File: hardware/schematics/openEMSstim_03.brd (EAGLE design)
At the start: 38 x 59 mm, 37 parts

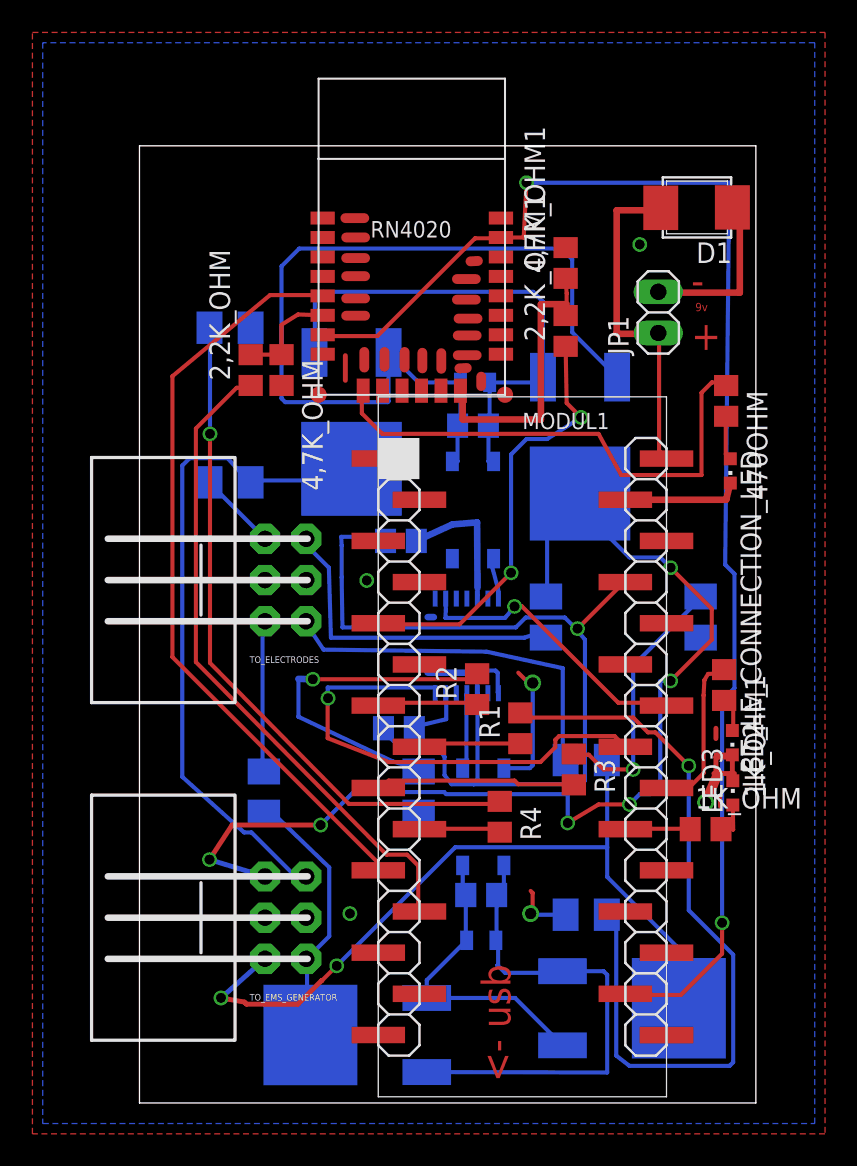
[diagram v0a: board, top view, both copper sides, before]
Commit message: new board design V3: not tested yet
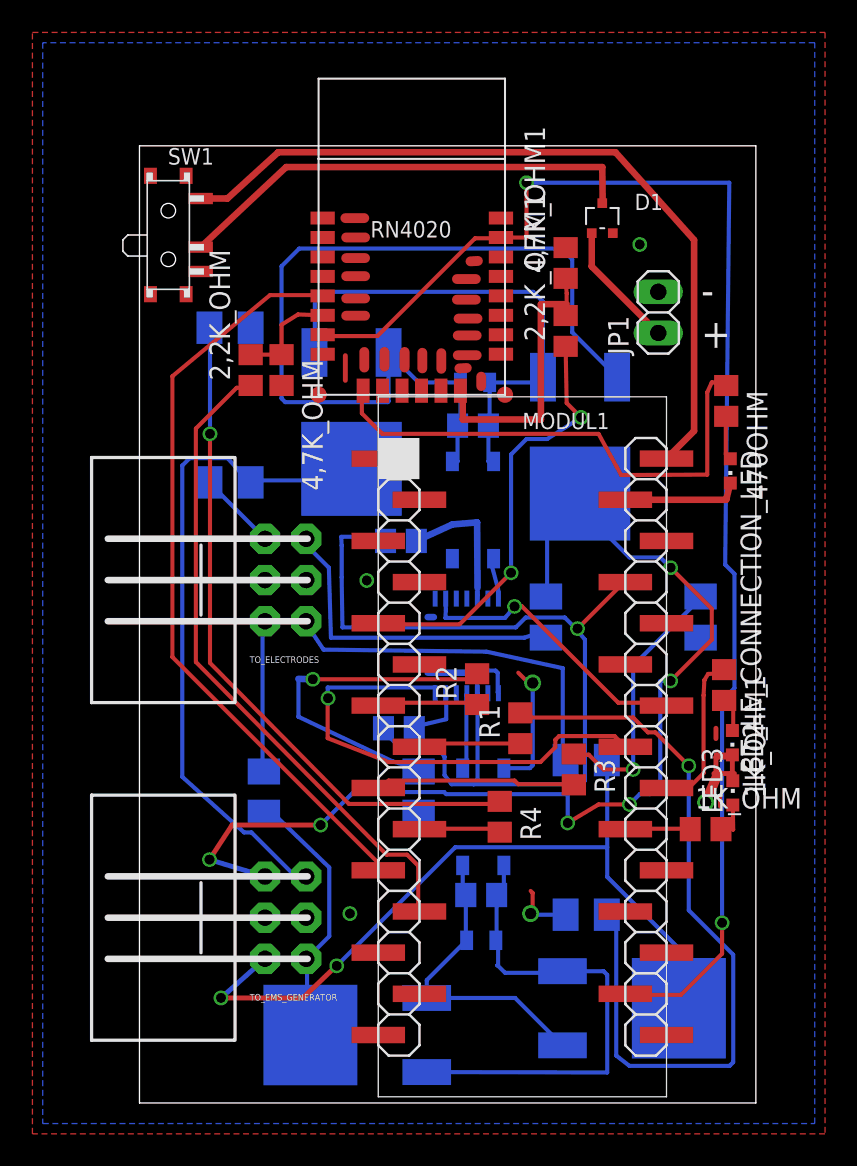
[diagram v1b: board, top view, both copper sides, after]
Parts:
- added SW1: SW1, alps:SSSS810701
- D1: value 1N4001 -> 1PS70SB10; device semicon-smd-ipc:SMB -> nxp_60:SOT323
- moved D1 5.74 mm to (32.6, 54.6), turned to 0 degrees
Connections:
- new net N$64: D1.3, SW1.2
- net N$11: now also SW1.1; no longer D1.1
- net N$63: now also D1.1; no longer D1.2
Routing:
- net N$11: track 7.76 -> 48.1 mm
- net N$64: track 12.5 -> 29.0 mm
- net N$65: track 10.8 -> 0.00 mm
- net N$63: track 0.00 -> 7.86 mm
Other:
- board text added: "- +"
- board text added: "open EMS stim"
- board text added: "openEMSstim v2 plopes.org/ems"
- board text removed: "+"
- board text removed: "-"
- board text removed: "9v"
- board text removed: "<- usb"
- board text removed: "openEMSstim 0.2 by Pedro Lopes plopes.org/ems open source control board for EMS units based on toolkit by Pfeiffer & Duente v0.1"
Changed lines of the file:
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@@
 <layer number="112" name="tSilk" color="7" fill="1" visible="no" active="yes"/>
 <layer number="113" name="IDFDebug" color="7" fill="1" visible="no" active="yes"/>
+<layer number="114" name="FRNTMAAT1" color="7" fill="1" visible="yes" active="yes"/>
+<layer number="115" name="FRNTMAAT2" color="7" fill="1" visible="yes" active="yes"/>
 <layer number="116" name="Patch_BOT" color="9" fill="4" visible="no" active="yes"/>
+<layer number="117" name="BACKMAAT1" color="7" fill="1" visible="yes" active="yes"/>
 <layer number="118" name="Rect_Pads" color="7" fill="1" visible="no" active="no"/>
+<layer number="119" name="KAP_TEKEN" color="7" fill="1" visible="yes" active="yes"/>
+<layer number="120" name="KAP_MAAT1" color="7" fill="1" visible="yes" active="yes"/>
 <layer number="121" name="_tsilk" color="7" fill="1" visible="no" active="yes"/>
 <layer number="122" name="_bsilk" color="7" fill="1" visible="no" active="yes"/>
@@
 <layer number="128" name="_bValues" color="7" fill="1" visible="no" active="yes"/>
 <layer number="129" name="Mask" color="7" fill="1" visible="no" active="yes"/>
+<layer number="130" name="SMDSTROOK" color="7" fill="1" visible="yes" active="yes"/>
 <layer number="131" name="tAdjust" color="7" fill="1" visible="no" active="yes"/>
 <layer number="132" name="bAdjust" color="7" fill="1" visible="no" active="yes"/>
@@
 <text x="5.461" y="0.889" size="1.778" layer="126" rot="MR90">HCI - Hannover</text>
 <text x="40.64" y="58.039" size="1.778" layer="126" rot="MR270">V002 EMS WS Module</text>
-<text x="4.8514" y="52.6288" size="0.508" layer="104" font="vector" ratio="9">openEMSstim 0.2
-by Pedro Lopes
-plopes.org/ems
-open source control
-board for EMS units
-based on toolkit by
-Pfeiffer &amp; Duente v0.1</text>
-<text x="38.1" y="46.4566" size="1.778" layer="1">+</text>
-<text x="38.1" y="49.8602" size="1.778" layer="1">-</text>
-<text x="38.354" y="48.8442" size="0.508" layer="1">9v</text>
-<text x="26.9494" y="1.2954" size="1.778" layer="1" rot="R90">&lt;- usb </text>
+<text x="35.5854" y="57.2516" size="0.508" layer="104" font="vector" ratio="9">openEMSstim v2
+plopes.org/ems</text>
+<text x="4.4704" y="19.5326" size="1.27" layer="104">open
+EMS
+stim</text>
+<text x="38.7096" y="46.5836" size="1.778" layer="21">-
++</text>
 </plain>
 <attributes>
@@
 <element name="C1" library="SparkFun-Passives" package="0805" value="100nf" x="25.146" y="10.033" rot="MR0"/>
 <element name="C3" library="SparkFun-Passives" package="0805" value="100nf" x="24.765" y="44.45" rot="MR0"/>
-<element name="D1" library="semicon-smd-ipc" package="SMB" value="1N4001" x="38.3286" y="55.118" rot="R180"/>
+<element name="D1" library="nxp_60" package="SOT323" value="1PS70SB10" x="32.6136" y="54.5846"/>
+<element name="SW1" library="alps" package="SSSS810701" value="SW1" x="5.842" y="53.5432" smashed="yes" rot="R270">
+<attribute name="NAME" x="5.8166" y="57.8866" size="1.016" layer="25"/>
+</element>
 </elements>
 <signals>
@@
 <via x="27.94" y="56.769" extent="1-16" drill="0.6096"/>
 <wire x1="18.7325" y1="47.3075" x2="24.765" y2="53.34" width="0.254" layer="1"/>
-<wire x1="26.363" y1="53.388" x2="27.765" y2="53.388" width="0.254" layer="1"/>
-<wire x1="27.765" y1="53.388" x2="27.94" y2="56.769" width="0.254" layer="1"/>
+<wire x1="26.363" y1="53.388" x2="27.9428" y2="53.388" width="0.254" layer="1"/>
+<wire x1="27.9428" y1="53.388" x2="27.94" y2="56.769" width="0.254" layer="1"/>
 <wire x1="40.4495" y1="56.769" x2="40.1955" y2="33.2105" width="0.254" layer="16"/>
 <wire x1="40.1955" y1="33.2105" x2="40.767" y2="32.639" width="0.254" layer="16"/>
@@
 <signal name="N$11">
 <contactref element="MODUL1" pad="30"/>
-<wire x1="36.1188" y1="40.2336" x2="36.1188" y2="47.3202" width="0.254" layer="1"/>
-<wire x1="36.576" y1="39.7764" x2="36.1188" y2="40.2336" width="0.254" layer="1"/>
-<wire x1="36.576" y1="39.7764" x2="36.576" y2="39.751" width="0.254" layer="1"/>
-<contactref element="D1" pad="1"/>
-<wire x1="40.64" y1="55.245" x2="36.576" y2="39.751" width="0" layer="19" extent="1-1"/>
+<contactref element="SW1" pad="1"/>
+<wire x1="7.842" y1="55.7932" x2="9.489" y2="55.7932" width="0.4064" layer="1"/>
+<wire x1="9.489" y1="55.7932" x2="12.6238" y2="58.6486" width="0.4064" layer="1"/>
+<wire x1="12.6238" y1="58.6486" x2="33.4264" y2="58.6486" width="0.4064" layer="1"/>
+<wire x1="33.4264" y1="58.6486" x2="38.2778" y2="53.2384" width="0.4064" layer="1"/>
+<wire x1="38.2778" y1="53.2384" x2="38.2778" y2="41.4528" width="0.4064" layer="1"/>
+<wire x1="38.2778" y1="41.4528" x2="36.576" y2="39.751" width="0.4064" layer="1"/>
 </signal>
 <signal name="N$17">
@@
 <wire x1="32.385" y1="41.275" x2="19.05" y2="41.275" width="0.254" layer="1"/>
 <wire x1="33.782" y1="38.735" x2="32.385" y2="41.275" width="0.254" layer="1"/>
-<wire x1="38.735" y1="38.735" x2="33.782" y2="38.735" width="0.254" layer="1"/>
-<wire x1="38.735" y1="43.815" x2="38.735" y2="38.735" width="0.254" layer="1"/>
-<wire x1="39.37" y1="44.45" x2="38.735" y2="43.815" width="0.254" layer="1"/>
+<wire x1="39.0906" y1="38.7604" x2="33.782" y2="38.735" width="0.254" layer="1"/>
+<wire x1="39.0906" y1="43.8404" x2="39.0906" y2="38.7604" width="0.254" layer="1"/>
+<wire x1="39.37" y1="44.45" x2="39.0906" y2="43.8404" width="0.254" layer="1"/>
 <wire x1="40.005" y1="44.45" x2="39.37" y2="44.45" width="0.254" layer="1"/>
 <wire x1="17.78" y1="43.815" x2="17.863" y2="43.938" width="0.254" layer="1"/>
@@
 <wire x1="18.0848" y1="32.1818" x2="18.0848" y2="32.2326" width="0.4064" layer="1"/>
 <wire x1="12.827" y1="44.262" x2="10.922" y2="47.823" width="0" layer="19" extent="1-16"/>
+<wire x1="26.363" y1="54.588" x2="30.353" y2="52.766" width="0" layer="19" extent="1-1"/>
 </signal>
 <signal name="N$2">
@@
 <wire x1="32.9184" y1="21.0312" x2="32.893" y2="21.153" width="0.254" layer="16"/>
 <wire x1="37.2618" y1="5.9436" x2="37.338" y2="5.842" width="0.254" layer="16"/>
-<wire x1="16.2306" y1="8.4582" x2="15.3162" y2="7.5438" width="0.254" layer="1"/>
+<wire x1="16.2306" y1="8.4582" x2="16.2052" y2="8.4582" width="0.254" layer="1"/>
 <wire x1="23.5458" y1="15.7734" x2="16.2306" y2="8.4582" width="0.254" layer="16"/>
 <wire x1="32.9184" y1="15.7734" x2="23.5458" y2="15.7734" width="0.254" layer="16"/>
 <via x="16.2306" y="8.4582" extent="1-16" drill="0.6096"/>
-<wire x1="15.3162" y1="7.5438" x2="15.2908" y2="7.5438" width="0.3048" layer="1"/>
-<wire x1="15.2908" y1="7.5438" x2="13.843" y2="6.096" width="0.3048" layer="1"/>
-<wire x1="13.843" y1="6.096" x2="10.668" y2="6.096" width="0.3048" layer="1"/>
-<wire x1="10.668" y1="6.096" x2="10.541" y2="6.223" width="0.3048" layer="1"/>
-<wire x1="10.541" y1="6.223" x2="9.0932" y2="6.477" width="0.3048" layer="1"/>
+<wire x1="16.2052" y1="8.4582" x2="14.1478" y2="6.477" width="0.3048" layer="1"/>
+<wire x1="14.1478" y1="6.477" x2="9.0932" y2="6.477" width="0.3048" layer="1"/>
 <via x="9.0932" y="6.477" extent="1-16" drill="0.6096"/>
 <wire x1="9.0932" y1="6.477" x2="11.809" y2="8.889" width="0.3048" layer="16"/>
@@
 <signal name="N$63">
 <contactref element="JP1" pad="1"/>
-<contactref element="D1" pad="2"/>
-<wire x1="36.2204" y1="55.2196" x2="36.068" y2="47.498" width="0" layer="19" extent="1-1"/>
+<contactref element="D1" pad="1"/>
+<wire x1="36.068" y1="47.498" x2="31.9636" y2="51.6024" width="0.4064" layer="1"/>
+<wire x1="31.9636" y1="51.6024" x2="31.9636" y2="53.6596" width="0.4064" layer="1"/>
 </signal>
 <signal name="N$64">
-<wire x1="35.9918" y1="47.4472" x2="33.5788" y2="47.4472" width="0.4064" layer="1"/>
-<wire x1="33.5788" y1="47.4472" x2="33.5788" y2="47.498" width="0.4064" layer="1"/>
-<wire x1="33.5788" y1="47.498" x2="33.5026" y2="47.498" width="0.4064" layer="1"/>
-<wire x1="33.5026" y1="47.498" x2="33.5026" y2="55.0672" width="0.4064" layer="1"/>
-<wire x1="33.5026" y1="55.0672" x2="35.8648" y2="55.0672" width="0.4064" layer="1"/>
-</signal>
-<signal name="N$65">
-<wire x1="36.0426" y1="49.9872" x2="41.0972" y2="49.9872" width="0.4064" layer="1"/>
-<wire x1="41.0972" y1="49.9872" x2="41.0972" y2="55.7784" width="0.4064" layer="1"/>
+<contactref element="D1" pad="3"/>
+<contactref element="SW1" pad="2"/>
+<wire x1="32.6136" y1="55.5096" x2="32.639" y2="55.535" width="0.4064" layer="1"/>
+<wire x1="32.639" y1="55.535" x2="32.6136" y2="57.7342" width="0.4064" layer="1"/>
+<wire x1="32.6136" y1="57.7342" x2="13.1132" y2="57.7342" width="0.4064" layer="1"/>
+<wire x1="13.1132" y1="57.7342" x2="7.842" y2="52.7932" width="0.4064" layer="1"/>
 </signal>
 </signals>
